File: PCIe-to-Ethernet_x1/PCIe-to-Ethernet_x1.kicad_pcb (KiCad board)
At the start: 4 copper layers, 65.3 x 64.4 mm, 77 parts, among them J1 1-406541-1, J1 PCIexpress_bracket, J2 Bus_PCI_Express_x1, T1 SM51625EL, Y1 WTL3M85411FO

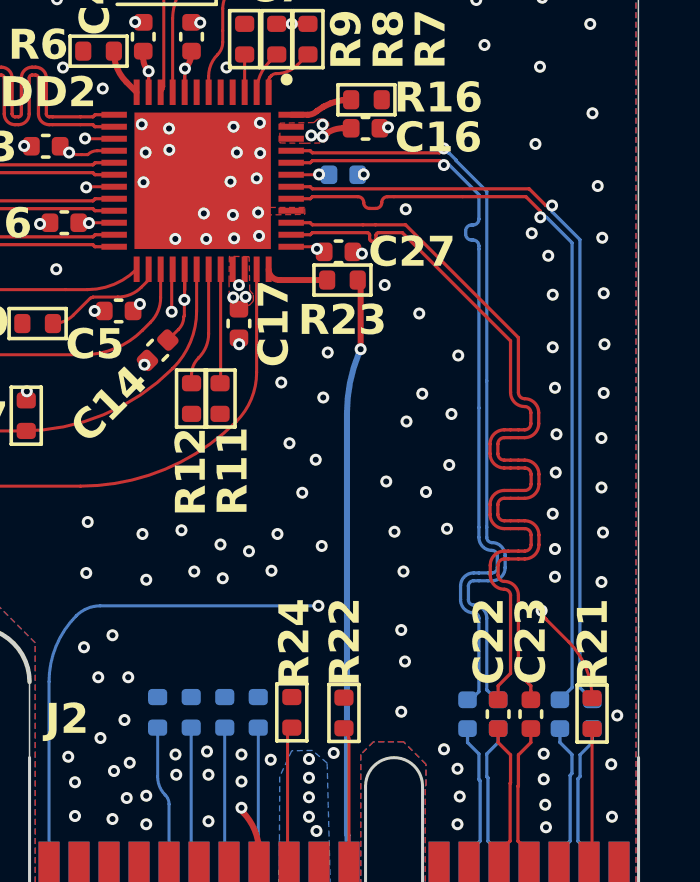
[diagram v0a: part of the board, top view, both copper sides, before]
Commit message: Исправил отсутствие перекрёстного соединения на  PCIe
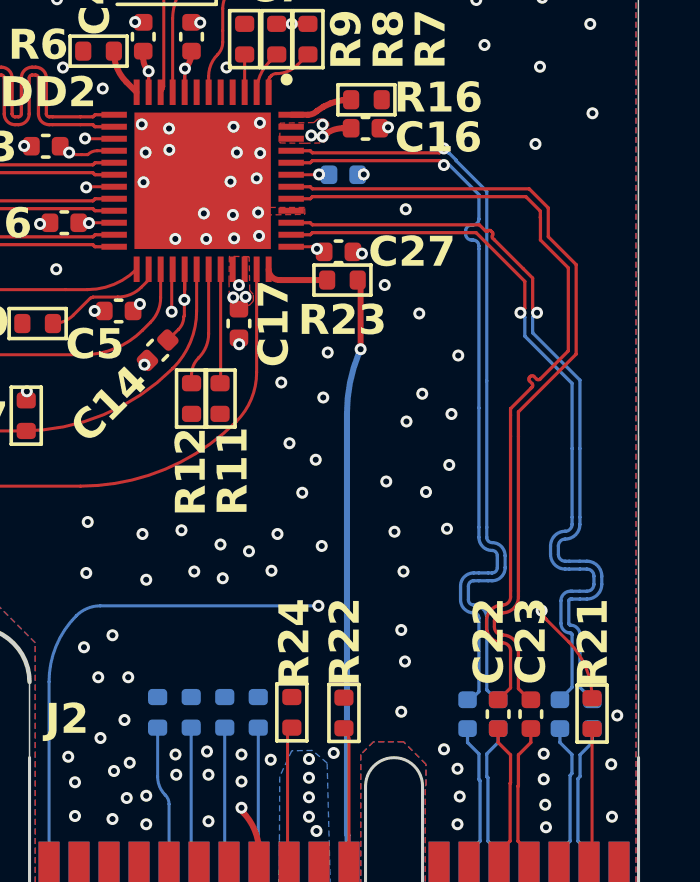
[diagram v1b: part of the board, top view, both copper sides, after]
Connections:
- C22 pad 1: PCIe_TX+ -> PCIe_RX+
- C23 pad 1: PCIe_TX- -> PCIe_RX-
- C24 pad 2: PCIe_RX+ -> PCIe_TX+
- C25 pad 2: PCIe_RX- -> PCIe_TX-
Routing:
- net PCIe_RX+: track 26.0 -> 27.5 mm, vias 1 -> 0
- net PCIe_RX-: track 26.0 -> 27.5 mm, vias 1 -> 0
- net PCIe_TX+: track 27.3 -> 25.9 mm, vias 0 -> 1
- net PCIe_TX-: track 27.3 -> 26.5 mm, vias 0 -> 1
- net Earth: vias 261 -> 242
